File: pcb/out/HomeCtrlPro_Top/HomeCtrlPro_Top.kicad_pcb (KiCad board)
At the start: 2 copper layers, 149.4 x 159 mm, 124 parts, among them J1 B2B, J10 RS485, J11 CAN, J12 TFT, J2 We 0-7, J3 We 8-15, J4 We 16-23, J5 We 24-31, J6 We 32-39, J7 We 40-47, J8 We 48-55, J9 We 56-63, SW1 RST, SW2 BOOT, SW3 GORA, SW4 DOL, SW5 OK, SW6 WSTECZ, U1 ESP32-S3-WROOM-1, U2 MCP23017, U3 MCP23017, U4 MCP23017, U5 MCP23017, U6 MAX485, U7 TJA1051

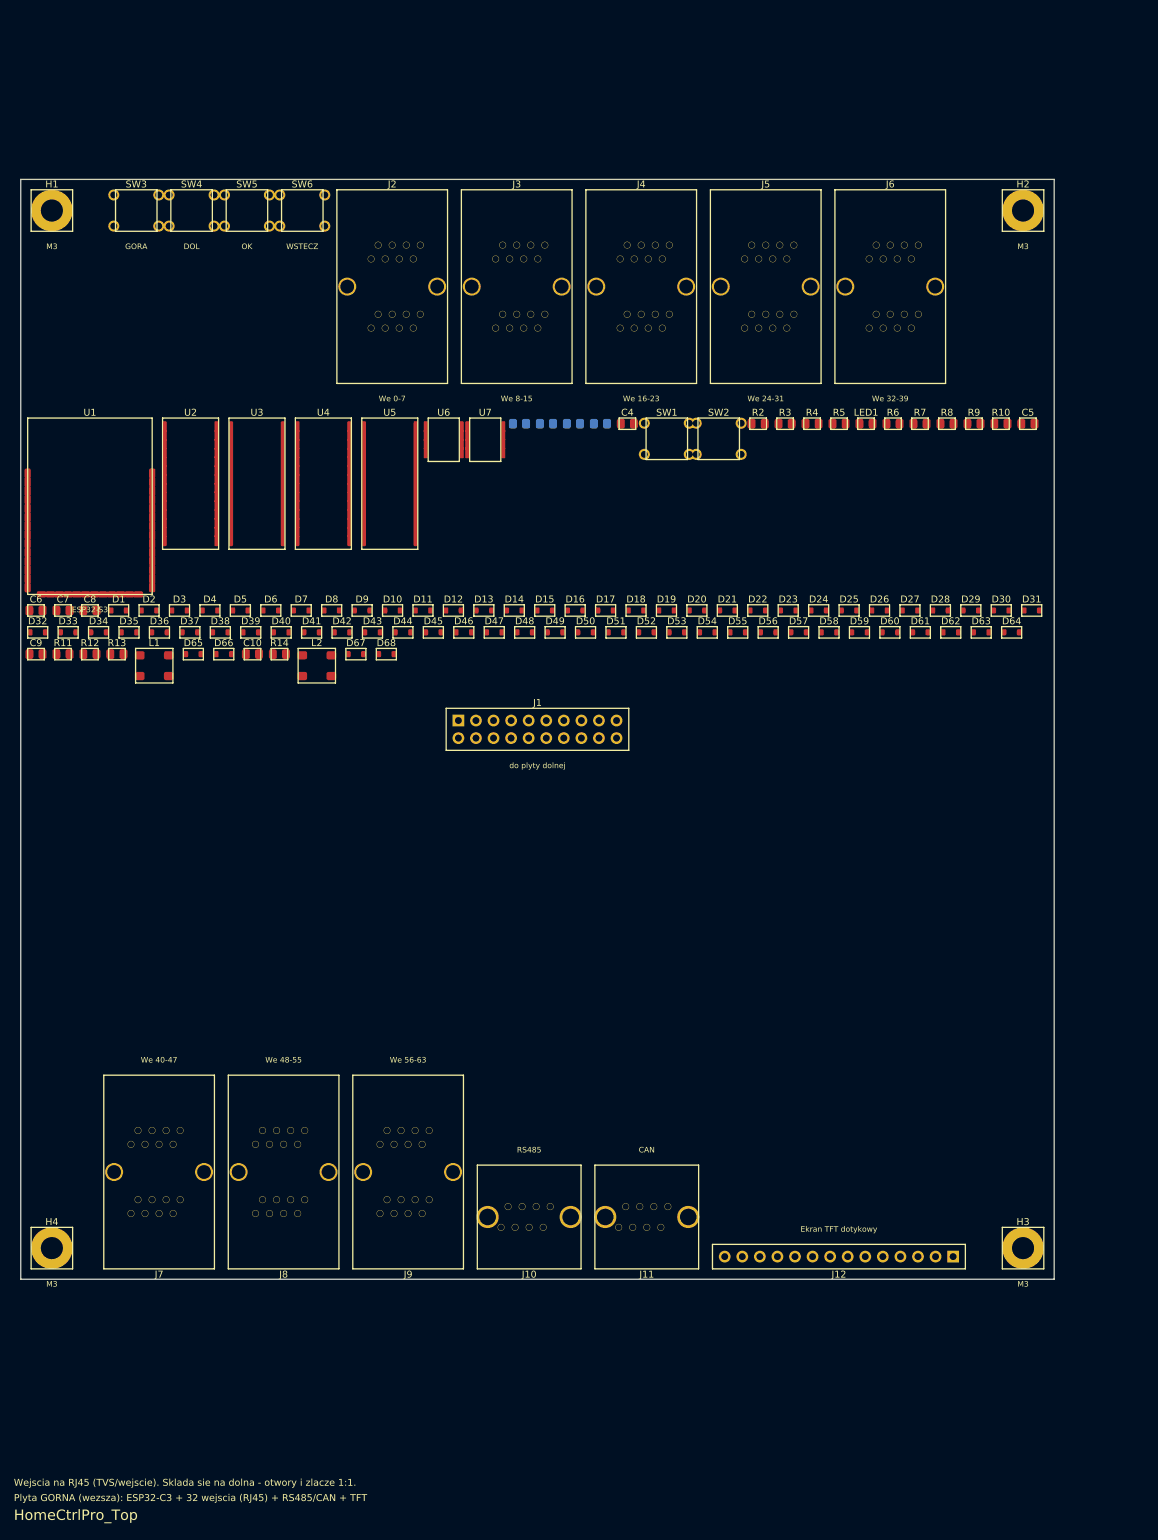
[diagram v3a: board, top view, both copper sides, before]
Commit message: Zageszczenie layoutu: ~2x mniejsza plytka (zajetosc 18% -> 38%)
- Pakowanie sortowane po wysokosci (wiersze o zblizonej wysokosci) - koniec z
  marnowaniem miejsca przez wysoki element w rzedzie.
- io_band = male wciecie (nie wysokosc zlacza); wysokie podwojne RJ45 mieszcza
  sie w srodku, nie rozdmuchuja pasow krawedziowych.
- Niezalezne wysokosci plyt (auto_layout) przy WSPOLNYCH otworach i B2B - mniejsza
  plyta nie dziedziczy wysokosci wiekszej.
- Wnetrze + przekazniki jako jeden ciasny blok; szerokosc wnetrza w estymacie =
  rzeczywista (koniec z przeszacowana wysokoscia/luka).
- Wysokie zlacza grupowane na jedna krawedz; TFT 2x07 (polowa szerokosci).

HomeCtrlPro DOL: 280x185 -> 168x100 mm. Oba 0/0/0, testy 12/12, kiutils OK.

Co-Authored-By: Claude Opus 4.8 (1M context) <noreply@anthropic.com>
Claude-Session: https://claude.ai/code/session_01LNGxtK2Jv1rJLBLPTwFQ9C
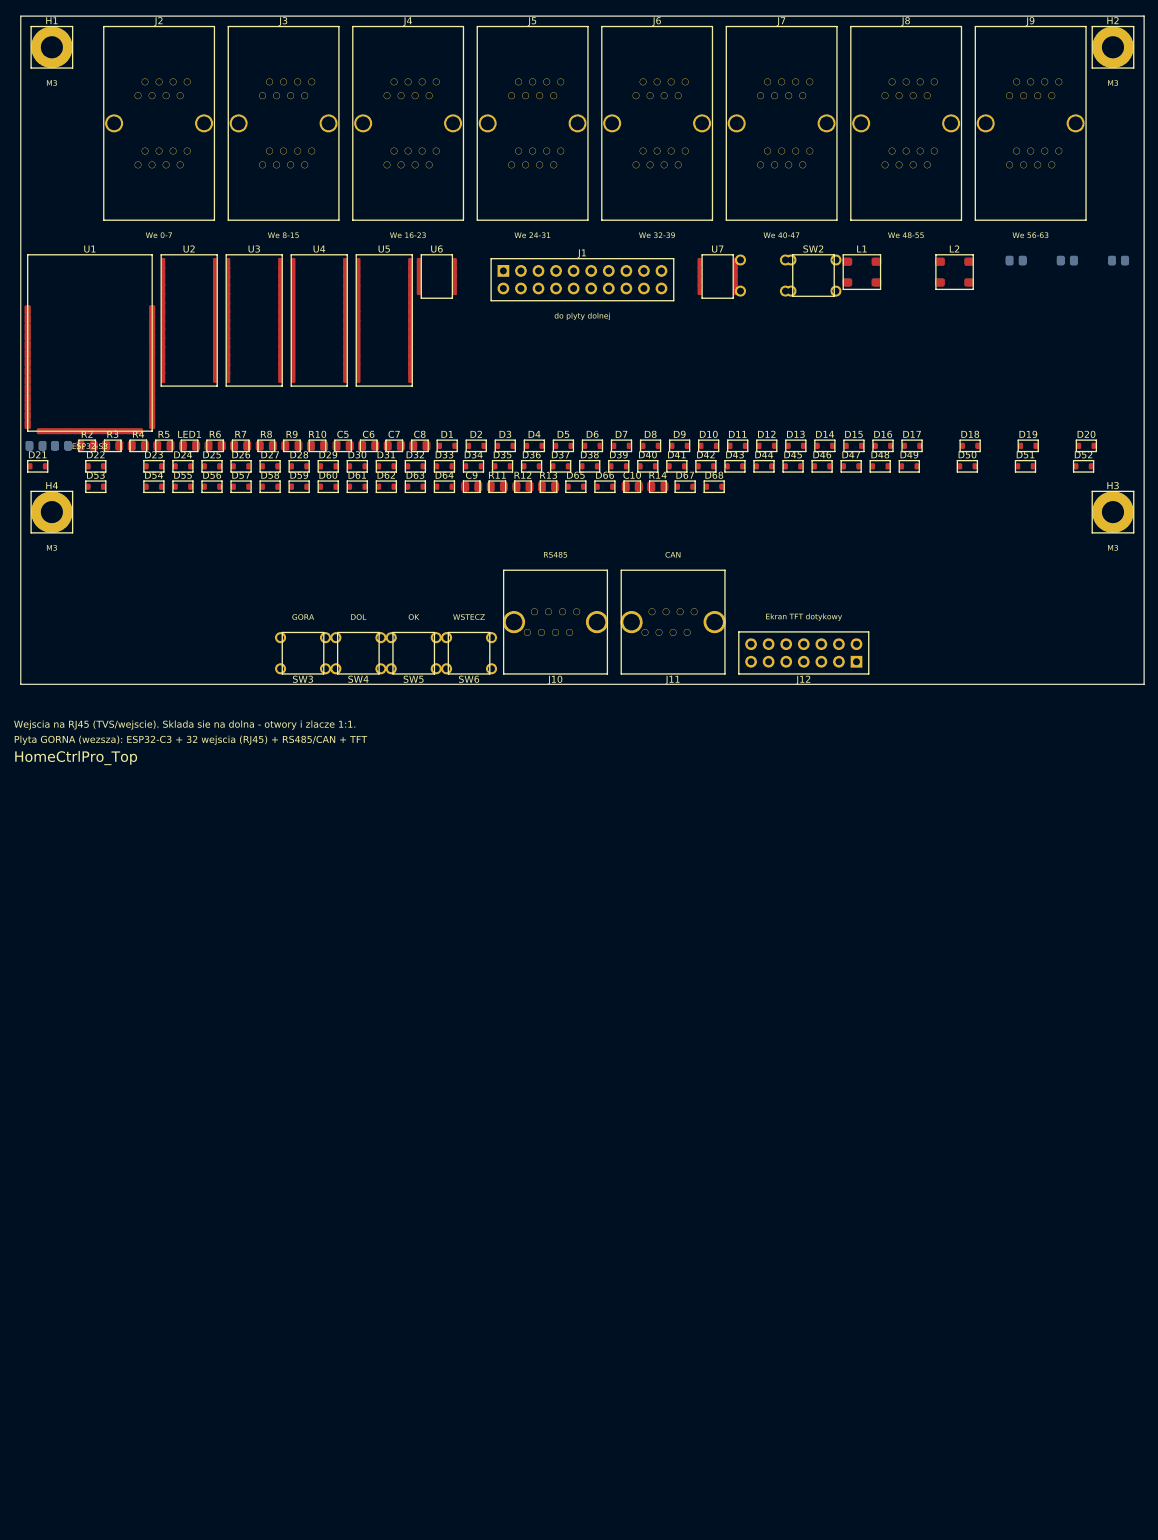
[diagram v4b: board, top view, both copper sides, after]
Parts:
- C4, SW1: moved to B.Cu
- J12: footprint pcbforge:PinHeader_1x14_P2.54mm -> pcbforge:PinHeader_2x07_P2.54mm
- moved J7 176.3 mm to (113.0, 27.5), turned to 0 degrees
- moved J8 176.3 mm to (131.0, 27.5), turned to 0 degrees
- moved J9 176.3 mm to (149.0, 27.5), turned to 0 degrees
- moved L1 117.1 mm to (124.6, 49.0)
- moved L2 108.3 mm to (138.0, 49.0)
- moved H3 107.2 mm to (160.9, 83.7)
- moved H4 106.4 mm to (7.50, 83.7)
- moved D21 101.9 mm to (5.45, 77.1)
- moved C5 99.1 mm to (49.6, 74.1)
- moved R10 98.9 mm to (45.9, 74.1)
- moved R9 98.7 mm to (42.2, 74.1)
- moved R8 98.5 mm to (38.5, 74.1)
- moved R7 98.3 mm to (34.8, 74.1)
- moved R6 98.1 mm to (31.1, 74.1)
- moved D22 97.9 mm to (13.8, 77.1)
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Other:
- board size 149.4 x 159 mm -> 162.4 x 96.6 mm

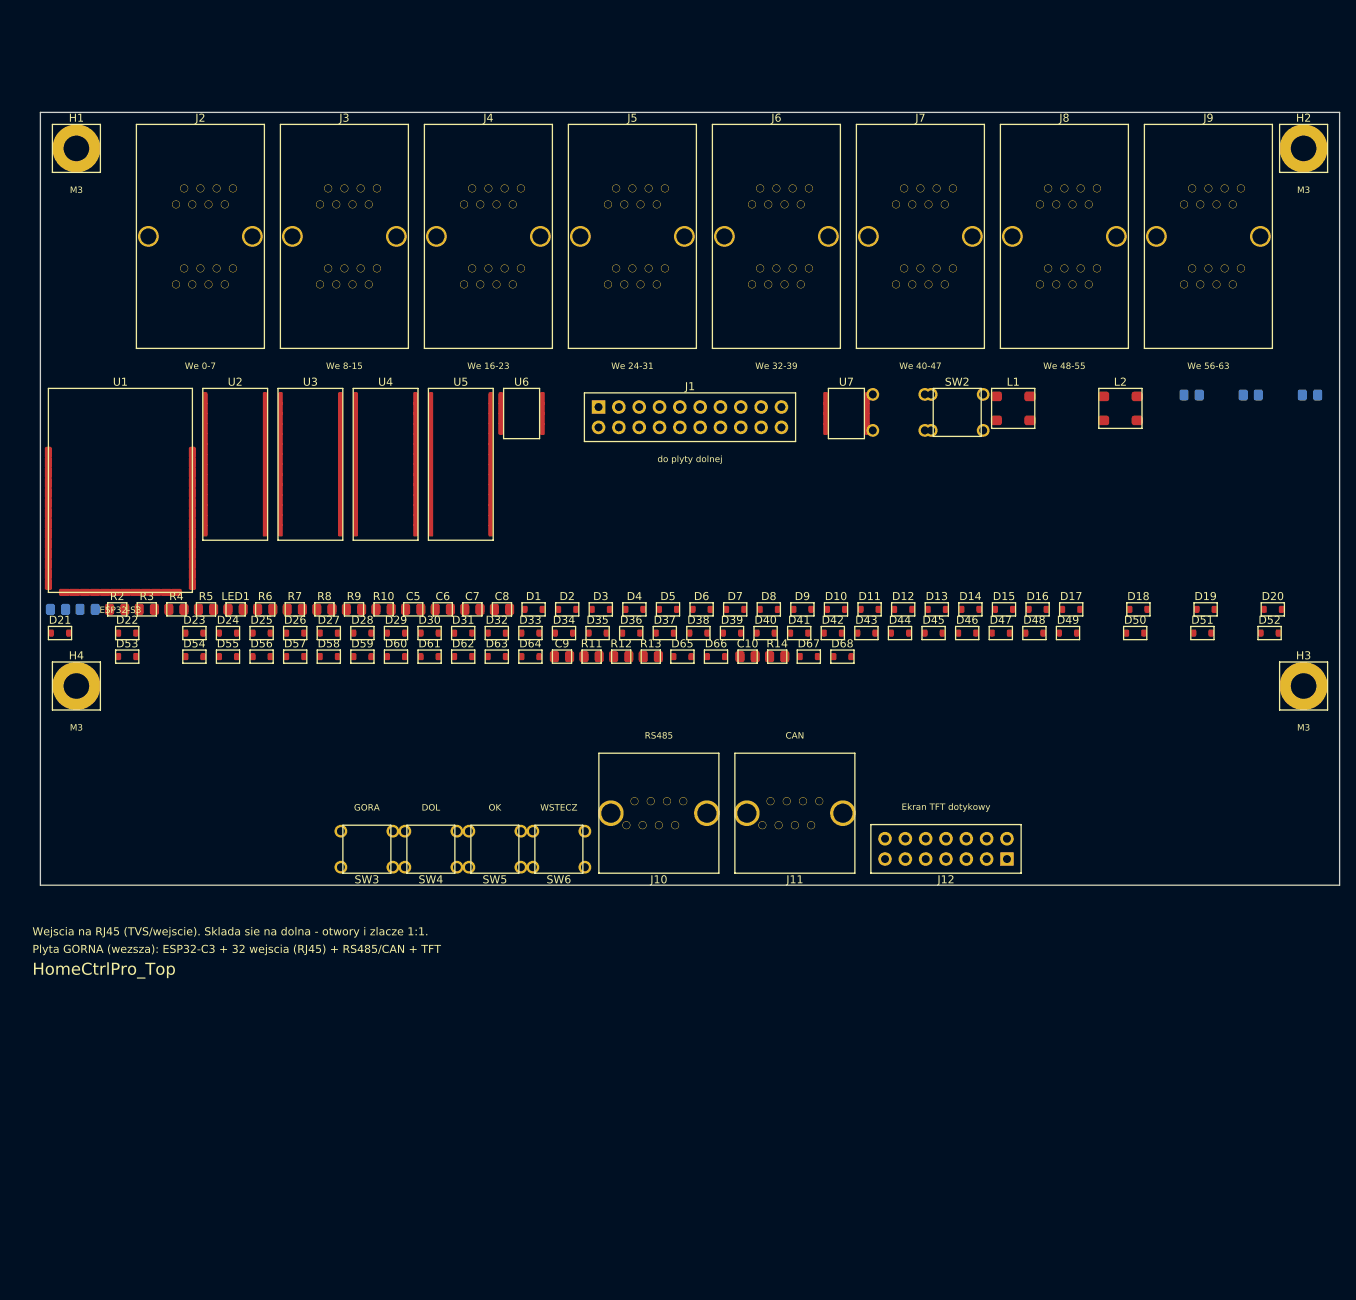
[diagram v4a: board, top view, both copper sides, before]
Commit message: Uklad na 4 krawedziach (plyta ~kwadratowa): wejscia gora+lewo, wyjscia dol+prawo
- Nowy tryb auto_layout_4e + place_board_4e: zlacza rozlozone na 4 krawedziach,
  zlacza na bokach obrocone 90/270 (_place_side), rotacjo-swiadome obrysy (_ext, DRC).
- Otwory w WEWNETRZNYCH narozach (wewnatrz pasow zlacz obu plyt) - brak kolizji
  otwor-zlacze; B2B w srodku. Wspolne wspolrzedne.
- _pack nigdy nie naklada (rosnie w dol zamiast nachodzic na przeszkody).
- Przyciski TFT przeniesione do wnetrza (przy ekranie).

HomeCtrlPro: zlacza na calym obwodzie, ~kwadrat 128x158 (z 280x185).
Oba PCB 0/0/0, testy 12/12, kiutils OK.

Co-Authored-By: Claude Opus 4.8 (1M context) <noreply@anthropic.com>
Claude-Session: https://claude.ai/code/session_01LNGxtK2Jv1rJLBLPTwFQ9C
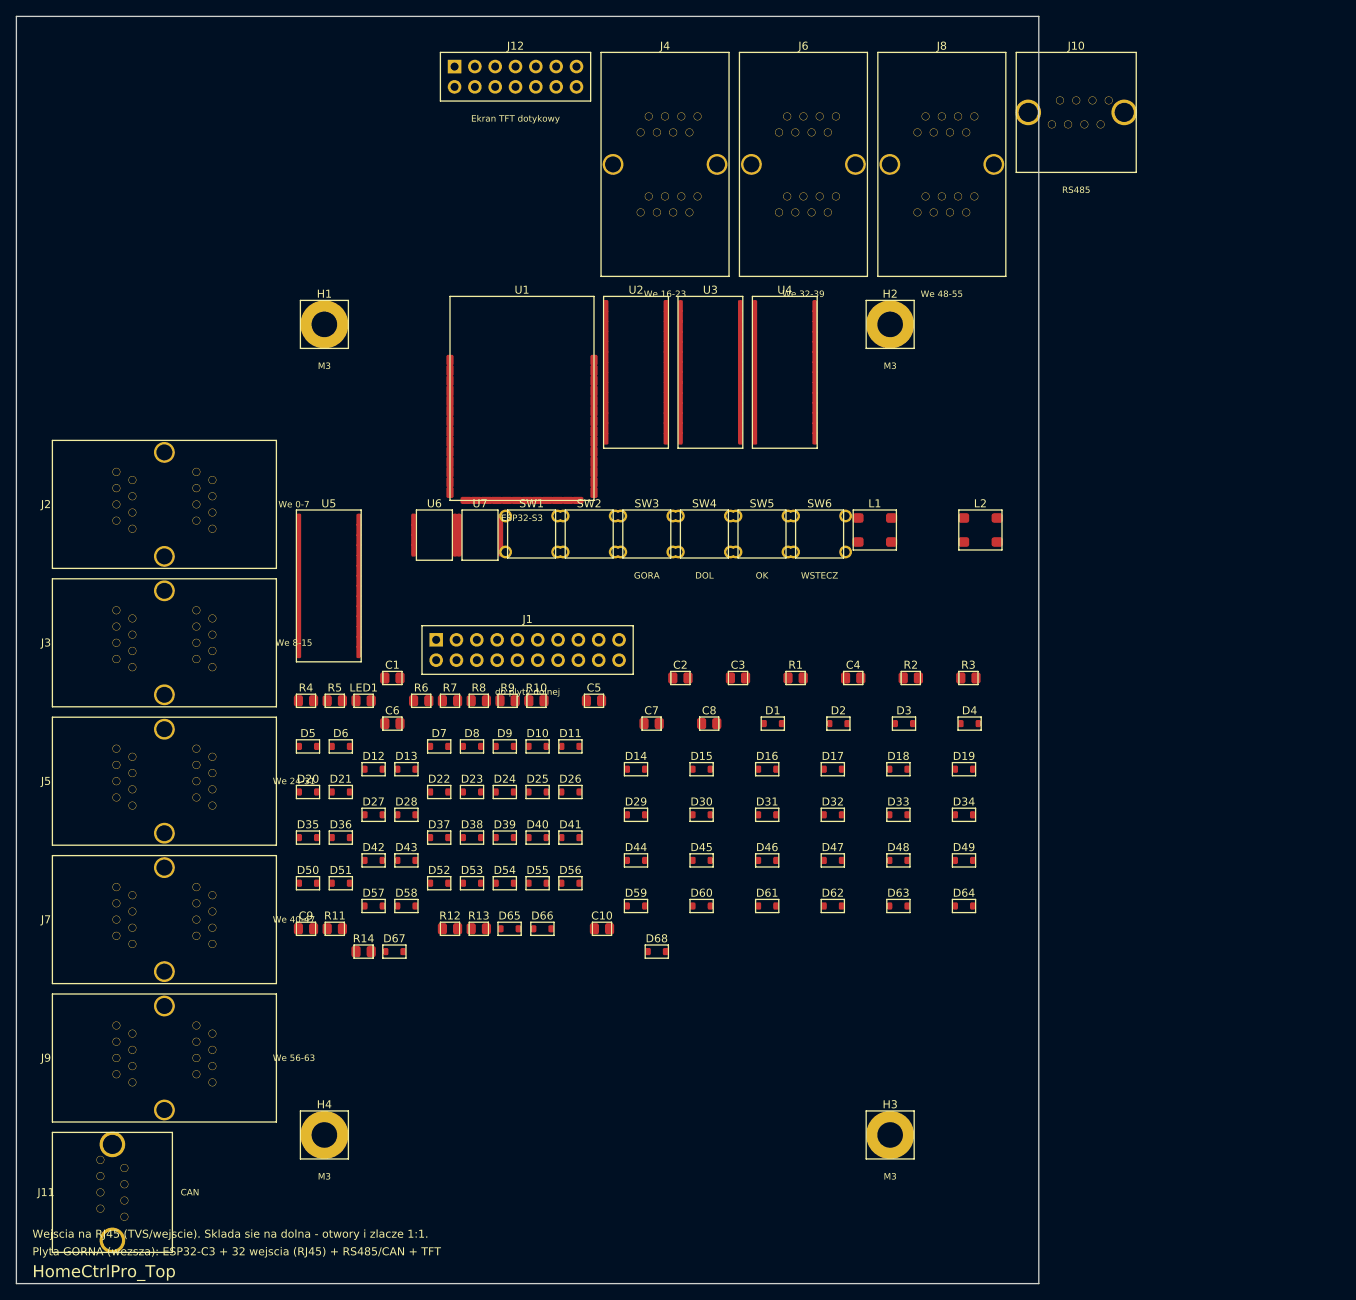
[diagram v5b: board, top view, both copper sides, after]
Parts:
- C1, C2, C3, C4, R1, SW1: moved to F.Cu
- moved J9 166.1 mm to (18.5, 130.2), turned to 90 degrees
- moved J7 127.4 mm to (18.5, 112.9), turned to 90 degrees
- moved D20 122.7 mm to (36.5, 97.0)
- moved D51 112.1 mm to (40.5, 108.3)
- moved J12 110.5 mm to (62.4, 7.54), turned to 0 degrees
- moved D52 108.4 mm to (52.9, 108.3)
- moved D50 108.0 mm to (36.5, 108.3)
- moved C1 106.0 mm to (47.0, 82.7)
- moved R3 103.1 mm to (119.0, 82.7)
- moved J10 102.0 mm to (132.5, 12.0), turned to 0 degrees
- moved R2 99.6 mm to (111.8, 82.7)
- moved J11 97.6 mm to (12.0, 147.0), turned to 90 degrees
- moved C4 96.1 mm to (104.6, 82.7)
- moved R1 92.6 mm to (97.4, 82.7)
- moved J5 89.8 mm to (18.5, 95.6), turned to 90 degrees
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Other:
- board size 162.4 x 96.6 mm -> 127.8 x 158.4 mm

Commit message: Uporzadkuj rozstaw R/C: grupowanie identycznych czesci w rowne rzedy
_pack sortuje po (wysokosc, szerokosc, typ, wartosc) - identyczne rezystory/
kondensatory/LED-y trafiaja obok siebie w regularnych rzedach zamiast losowego
wymieszania. Czytelniejszy, uporzadkowany uklad wnetrza. Oba PCB 0/0/0, testy 12/12.

Co-Authored-By: Claude Opus 4.8 (1M context) <noreply@anthropic.com>
Claude-Session: https://claude.ai/code/session_01LNGxtK2Jv1rJLBLPTwFQ9C
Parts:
- moved R5 83.2 mm to (119.0, 111.2)
- moved D20 82.4 mm to (118.5, 88.4)
- moved D35 82.4 mm to (118.5, 94.1)
- moved D50 82.4 mm to (118.5, 99.8)
- moved D5 78.4 mm to (114.3, 82.7)
- moved R3 65.6 mm to (61.4, 114.0)
- moved D65 57.4 mm to (118.5, 105.5)
- moved LED1 56.6 mm to (93.8, 111.2)
- moved C4 52.1 mm to (59.3, 108.3)
- moved C9 43.3 mm to (79.4, 111.2)
- moved C3 43.0 mm to (55.7, 108.3)
- moved R4 40.5 mm to (65.0, 114.0)
- moved C2 40.2 mm to (52.1, 108.3)
- moved D68 36.4 mm to (44.6, 108.3)
- moved R10 33.7 mm to (47.0, 114.0)
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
